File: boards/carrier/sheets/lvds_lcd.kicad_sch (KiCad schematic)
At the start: 4 parts

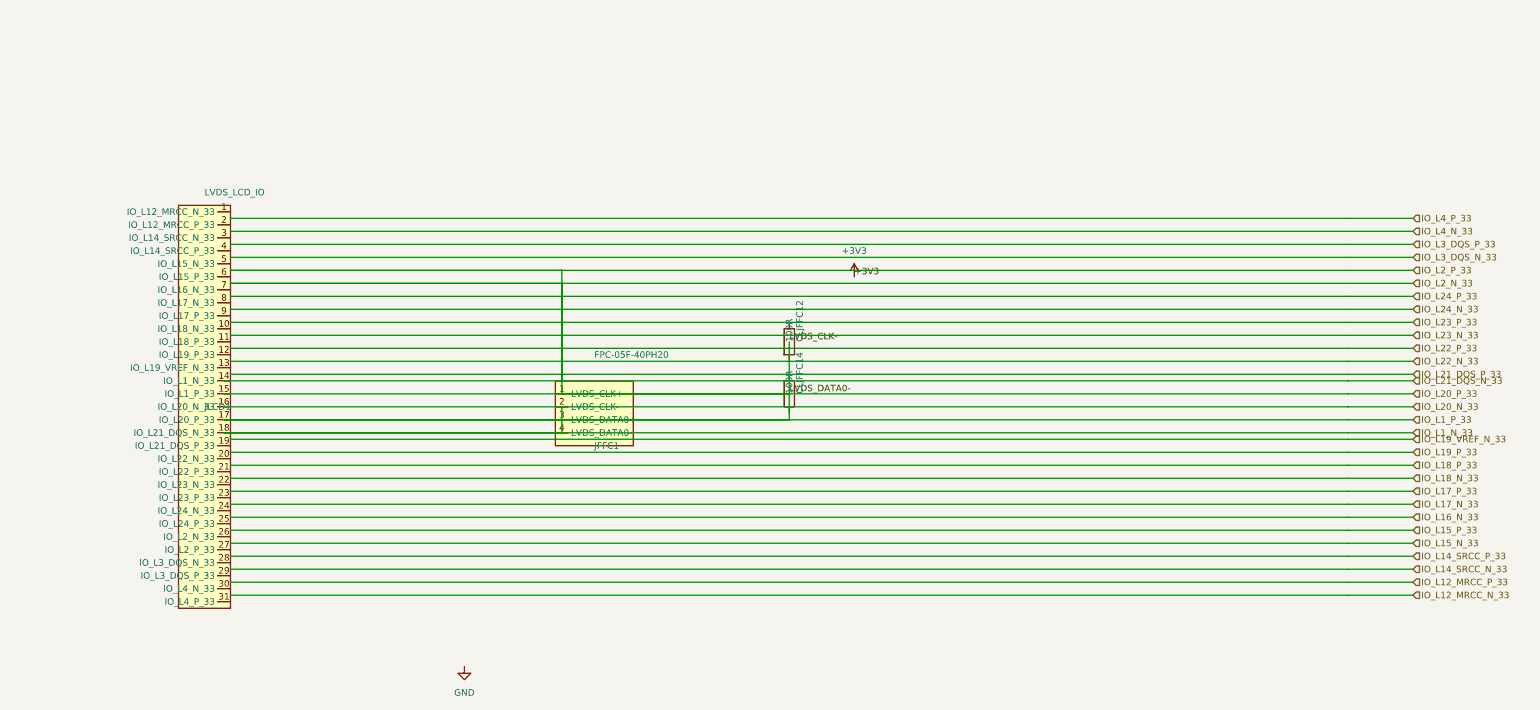
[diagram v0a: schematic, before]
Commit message: hdmi: use Connector_Generic:Conn_01x19 (Connector lib not auto-discovered)
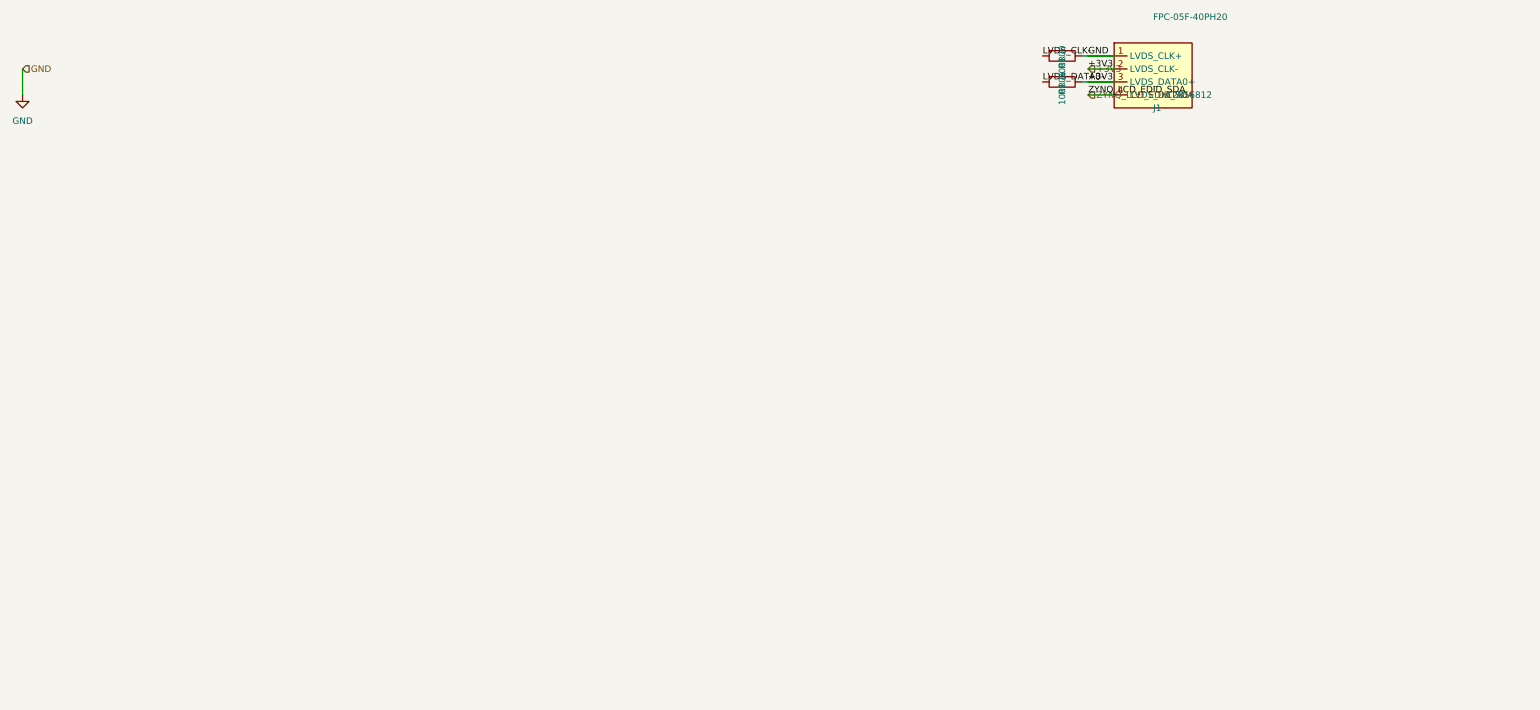
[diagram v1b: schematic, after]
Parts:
- removed CLJFFC12, CLJFFC14: 100R, Resistor_SMD:R_0402_1005Metric, symbol Device:R
- removed JFFC1: FPC-05F-40PH20, Connector_FFC-FPC:FPC-05F-40PH20, symbol carrier:FFC_40P
- removed JLCD1: LVDS_LCD_IO, symbol LVDS_LCD_IO:LVDS_LCD_IO
- added J1: FPC-05F-40PH20, Connector_FFC-FPC:FPC-05F-40PH20, symbol zynq_eda:FFC_40P
- added R100, R101: 100R, Resistor_SMD:R_0402_1005Metric, symbol Device:R
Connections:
- net +3V3: now also J1.2 (LVDS_CLK-), J1.3 (LVDS_DATA0+), R101.1
- net GND: now also J1.1 (LVDS_CLK+), R100.1
- new net LVDS_CLK-: R100.2
- new net LVDS_DATA0-: R101.2
- new net ZYNQ_LCD_EDID_SDA: J1.4 (LVDS_DATA0-)
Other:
- title: LVDS LCD FFC -> LVDS LCD (40-pin 0.5 mm FFC)
